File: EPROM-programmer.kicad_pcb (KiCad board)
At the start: 4 copper layers, 99.1 x 99.1 mm, 80 parts, among them J1 ZIF-socket, J10 VCC, J2 ISP, J5 GND, J6 Barrel_Jack_Switch, J7 ZIF_VCC, J8 VPP, J9 GND, P1 USB-C, Q1 BC327, Q2 BC327, Q3 BC327, Q4 BC327, Q5 BC327, Q6 BC327, SW1 SW_Push, U1 ATmega1284-P, U2 MCP2221AxP, U3 MCP4812, U4 LM358, U5 ULN2003, U6 LM317_TO-220, U7 LM317_TO-220, U8 R-78K9.0-0.5, Y1 20M

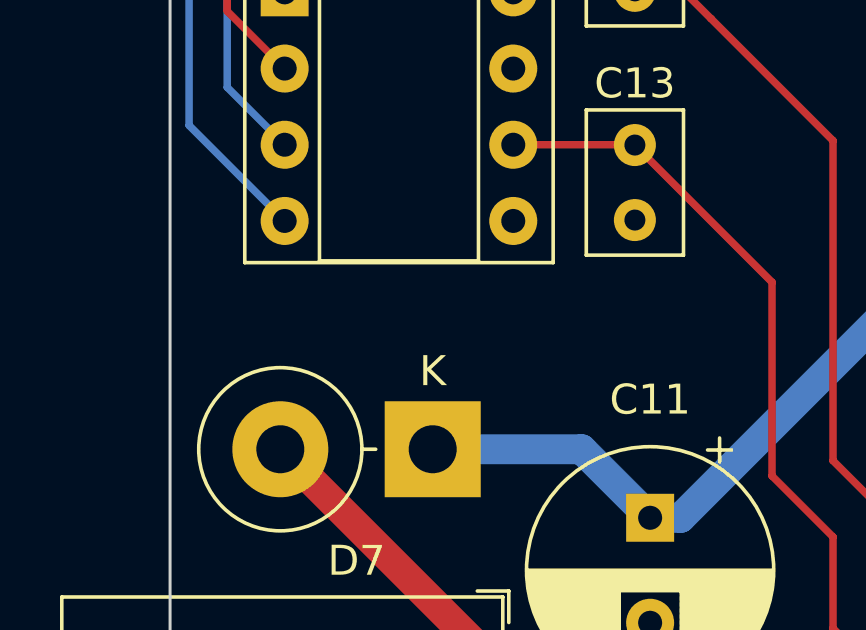
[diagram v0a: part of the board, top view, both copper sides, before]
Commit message: Add info about polarity and voltage to PCB
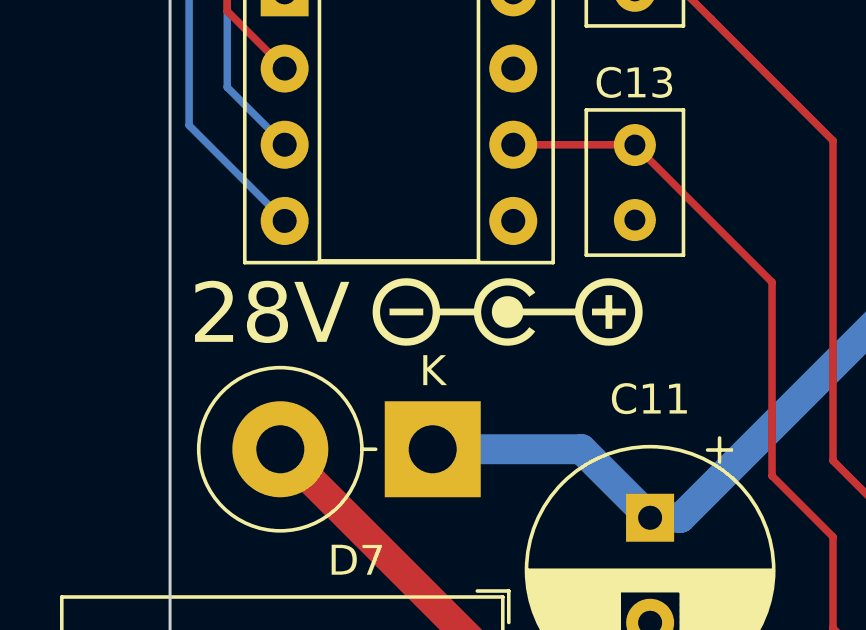
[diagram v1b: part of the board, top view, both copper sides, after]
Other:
- board text added: "28V"

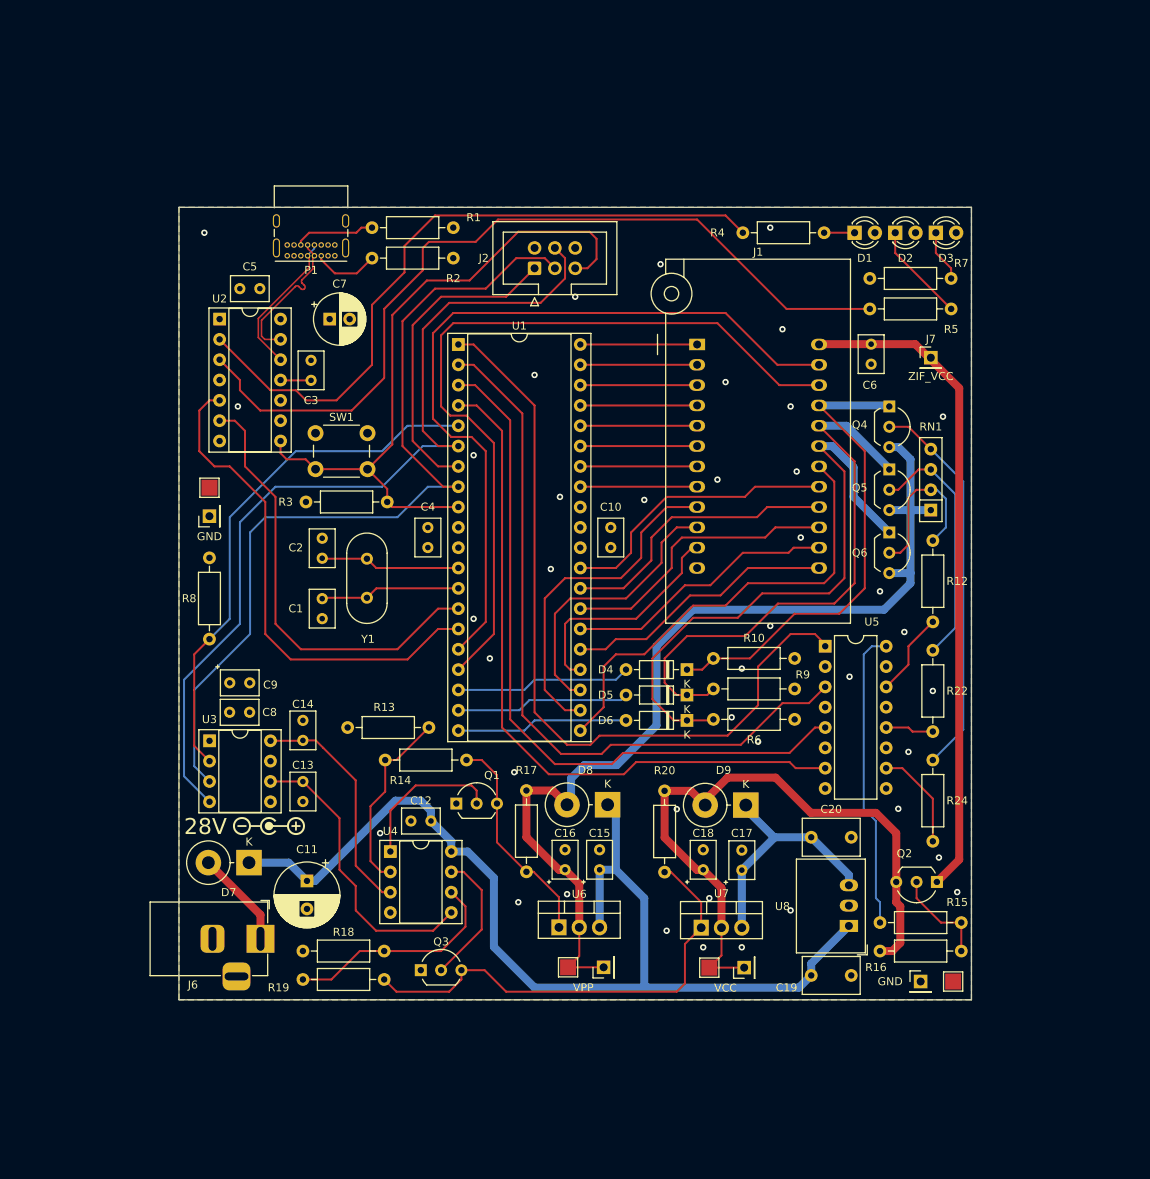
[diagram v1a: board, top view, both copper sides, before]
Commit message: Prepare for using 2 layers instead of 4
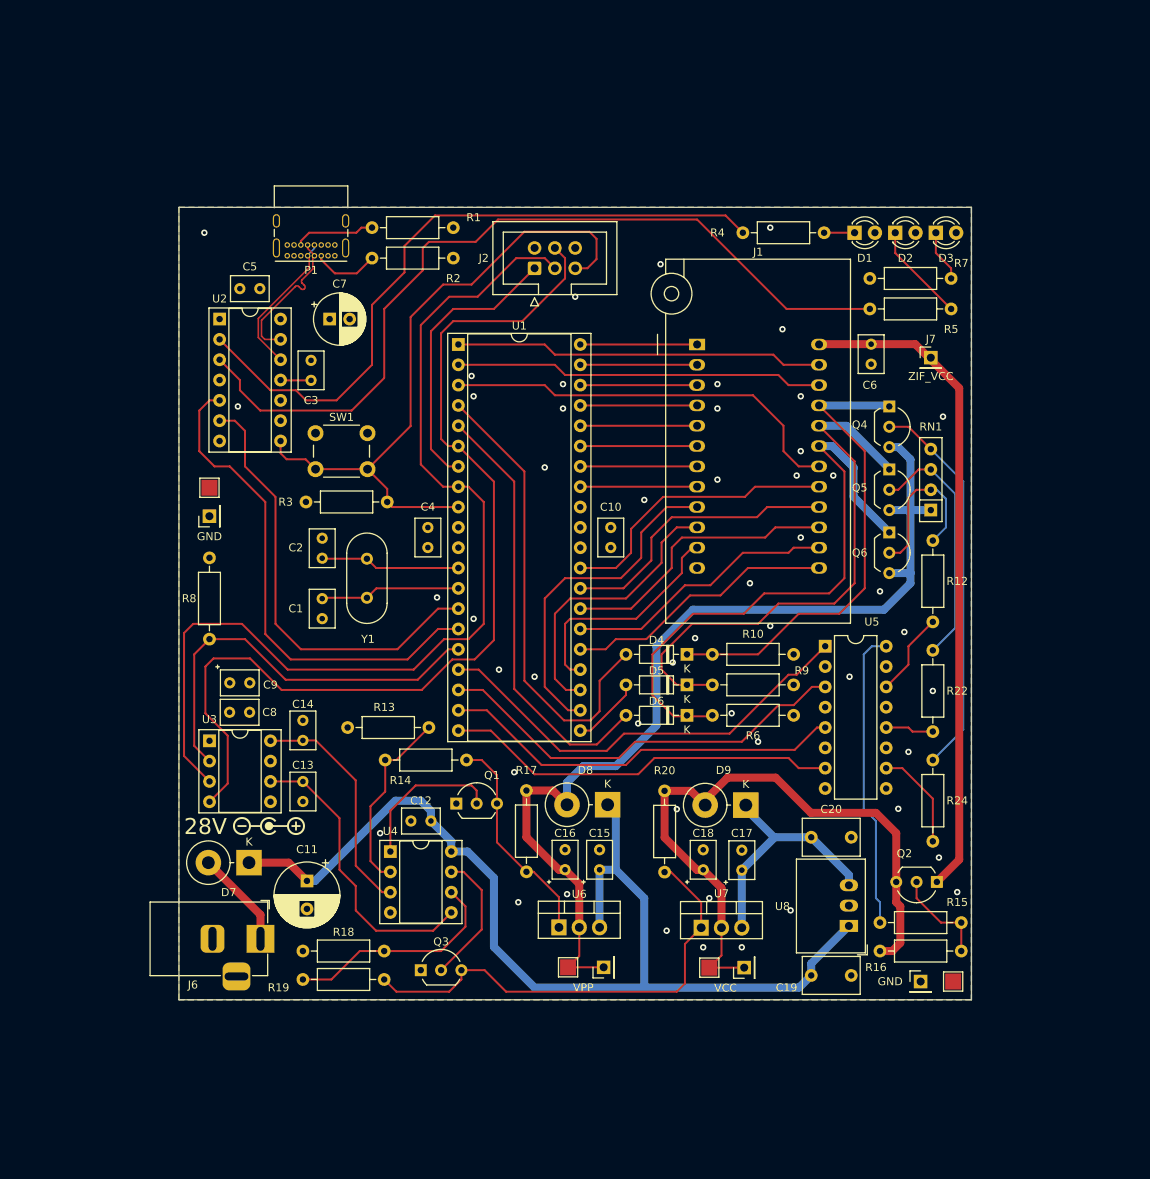
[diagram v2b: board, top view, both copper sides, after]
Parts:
- moved D4 1.91 mm to (102.9, 114.3)
- moved D5 1.27 mm to (102.9, 118.1)
- moved D6 0.64 mm to (102.9, 121.9)
- moved R10 0.52 mm to (106.0, 114.3)
- moved R6 0.52 mm to (106.0, 121.9)
- moved R9 0.52 mm to (106.0, 118.1)
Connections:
- U1 pad 1: /ZIF_VCC_EN -> /ZIF_P23
- U1 pad 16: /ZIF_P23 -> /~{SS}
- U1 pad 17: /ZIF_P22 -> /ZIF_VCC_EN
- U1 pad 18: /D_P21 -> /ZIF_VPP_P19_EN
- U1 pad 19: /D_P20 -> /ZIF_VPP_P20_EN
- U1 pad 2: /ZIF_VPP_P19_EN -> /ZIF_P22
- U1 pad 20: /D_P19 -> /ZIF_VPP_P21_EN
- U1 pad 21: /ZIF_P18 -> /D_P20
- U1 pad 3: /ZIF_VPP_P20_EN -> /ZIF_P18
- U1 pad 4: /ZIF_VPP_P21_EN -> /D_P21
- U1 pad 5: /~{SS} -> /D_P19
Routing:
- net /ZIF_P22: track 98.6 -> 46.1 mm
- net /ZIF_P23: track 97.1 -> 46.1 mm
- net /ZIF_VCC_EN: track 98.4 -> 55.5 mm
- net /ZIF_VPP_P20_EN: track 89.3 -> 50.6 mm
- net /ZIF_VPP_P19_EN: track 91.6 -> 53.1 mm
- net /ZIF_VPP_P21_EN: track 87.6 -> 49.5 mm
- net /D_P21: track 22.0 -> 58.2 mm
- net /D_P19: track 21.5 -> 54.1 mm
- net /SCK: track 110.8 -> 125.8 mm
- net /~{SS}: track 66.4 -> 51.6 mm
- net /D_P20: track 21.7 -> 8.83 mm
- net /MOSI: track 113.1 -> 124.2 mm
- net /ZIF_P18: track 57.0 -> 51.2 mm
- net /MISO: track 39.7 -> 35.3 mm
- net /~{RESET}: track 83.9 -> 82.4 mm
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
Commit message: Increase PCB size. Rework PCB to use 2 layers
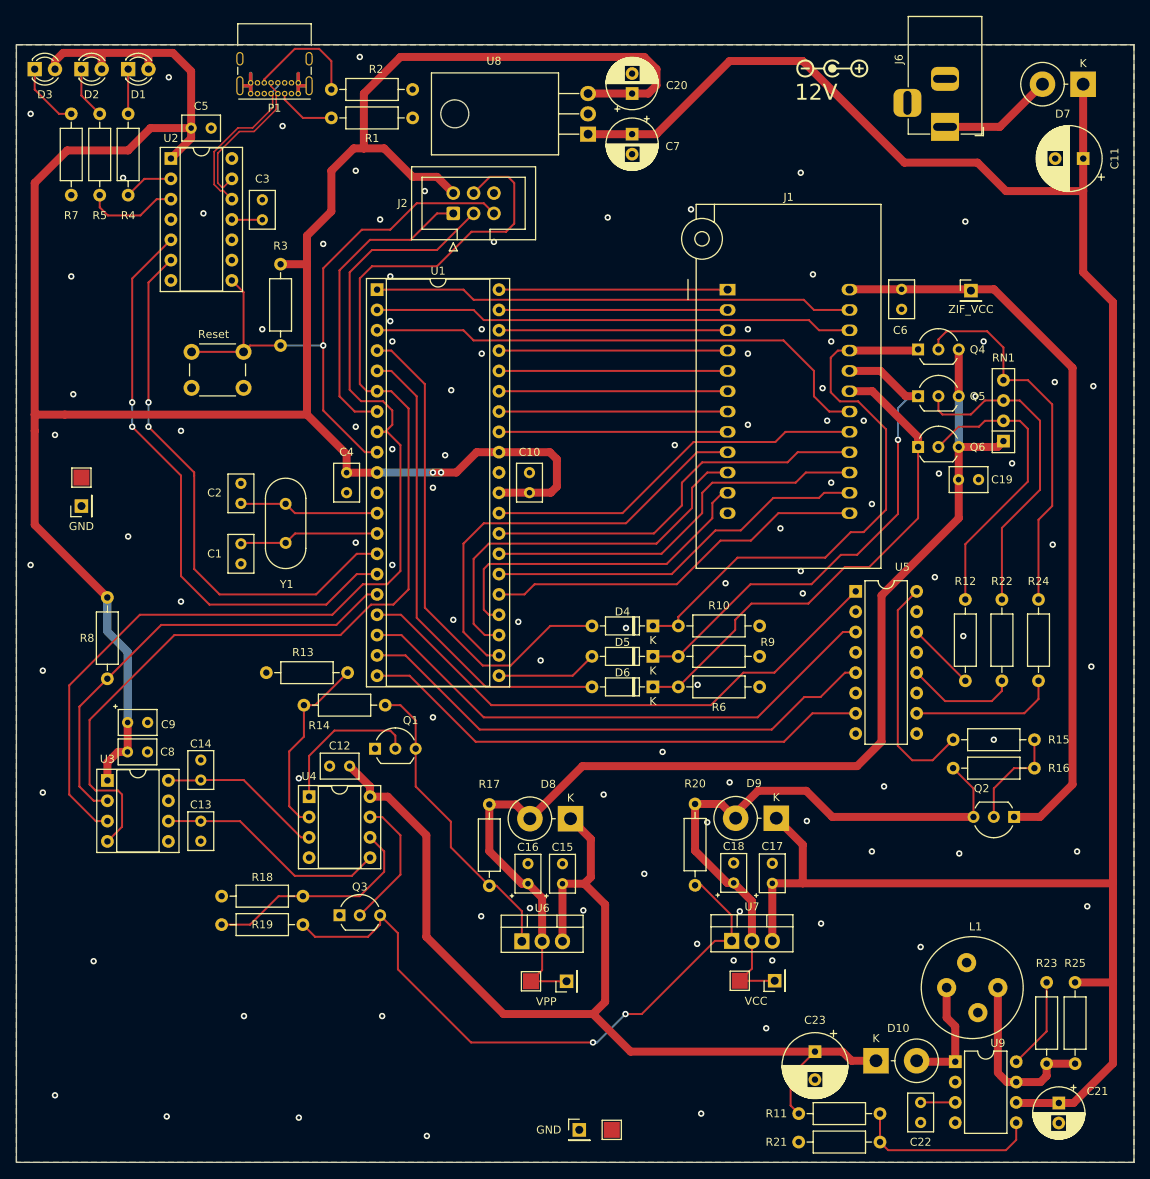
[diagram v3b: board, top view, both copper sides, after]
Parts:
- added C21: 100u, Capacitor_THT:CP_Radial_D6.3mm_P2.50mm, F.Cu at (149.4, 170.4)
- added C22: 270p, Capacitor_THT:C_Rect_L4.6mm_W3.0mm_P2.50mm_MKS02_FKP02, F.Cu at (132.1, 170.3)
- added C23: 330u, Capacitor_THT:CP_Radial_D8.0mm_P3.50mm, F.Cu at (118.9, 164.0)
- added D10: SB340, Diode_THT:D_DO-201AD_P5.08mm_Vertical_KathodeUp, F.Cu at (126.5, 165.1)
- added L1: 330u, Local:L_Radial_D12.5mm_P4.00mm_5.00mm, F.Cu at (140.7, 153.2)
- added R11: 22K1, Resistor_THT:R_Axial_DIN0207_L6.3mm_D2.5mm_P10.16mm_Horizontal, F.Cu at (127.0, 171.7)
- added R21: 1K, Resistor_THT:R_Axial_DIN0207_L6.3mm_D2.5mm_P10.16mm_Horizontal, F.Cu at (116.8, 175.3)
- added R23: 180, Resistor_THT:R_Axial_DIN0207_L6.3mm_D2.5mm_P10.16mm_Horizontal, F.Cu at (147.8, 155.3)
- added R25: R270, Resistor_THT:R_Axial_DIN0207_L6.3mm_D2.5mm_P10.16mm_Horizontal, F.Cu at (151.4, 155.3)
- added U9: MC34063AP, Package_DIP:DIP-8_W7.62mm, F.Cu at (136.4, 165.2)
- C19: value 10u -> 100n; footprint Capacitor_THT:C_Rect_L7.0mm_W4.5mm_P5.00mm -> Capacitor_THT:C_Rect_L4.6mm_W3.0mm_P2.50mm_MKS02_FKP02
- C20: value 22u -> 10u; footprint Capacitor_THT:C_Rect_L7.0mm_W4.5mm_P5.00mm -> Capacitor_THT:CP_Radial_D6.3mm_P2.50mm
- SW1: value SW_Push -> Reset
- U8: value R-78K9.0-0.5 -> LM7805_TO220; footprint Converter_DCDC:Converter_DCDC_RECOM_R-78E-0.5_THT -> Package_TO_SOT_THT:TO-220-3_Horizontal_TabDown
- moved D7 142.6 mm to (152.4, 43.0)
- moved J6 132.8 mm to (135.1, 48.4), turned to -90 degrees
- moved C11 132.5 mm to (152.4, 52.3), turned to 180 degrees
- moved D3 114.5 mm to (21.3, 41.1)
- moved R7 111.9 mm to (25.9, 46.7), turned to -90 degrees
- moved R5 109.2 mm to (29.5, 46.7), turned to -90 degrees
- moved U8 104.2 mm to (90.5, 49.3)
- moved D2 103.8 mm to (27.2, 41.1)
- moved C20 95.6 mm to (96.0, 44.2), turned to 90 degrees
- moved D1 93.1 mm to (33.0, 41.1)
- moved R4 88.3 mm to (33.0, 46.7), turned to -90 degrees
- moved C19 64.7 mm to (136.8, 92.5)
- moved J5 46.5 mm to (89.4, 173.7)
- moved TP3 46.5 mm to (93.5, 173.7)
- moved C7 44.3 mm to (96.0, 49.3), turned to -90 degrees
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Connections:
- net /28V_IN renamed /Power/12V_IN
- net /ADJ_VCC renamed /Power/ADJ_VCC
- net /ADJ_VPP renamed /Power/ADJ_VPP
- net /D+ renamed /Programmer/D+
- net /D- renamed /Programmer/D-
- net /DAC_VCC renamed /Power/DAC_VCC
- net /DAC_VPP renamed /Power/DAC_VPP
- net /D_P19 renamed /Programmer/D_P19
- net /D_P20 renamed /Programmer/D_P20
- net /D_P21 renamed /Programmer/D_P21
- net /FB_VCC renamed /Power/FB_VCC
- net /FB_VPP renamed /Power/FB_VPP
- net /MISO renamed /Programmer/MISO
- net /MOSI renamed /Programmer/MOSI
- net /RXD renamed /Programmer/RXD
- net /RXD_LED renamed /Programmer/RXD_LED
- net /SCK renamed /Programmer/SCK
- net /TXD renamed /Programmer/TXD
- net /TXD_LED renamed /Programmer/TXD_LED
- net /VCC renamed /Power/VCC
- net /XTAL1 renamed /Programmer/XTAL1
- net /XTAL2 renamed /Programmer/XTAL2
- net /ZIF_P1 renamed /Programmer/ZIF_P1
- net /ZIF_P10 renamed /Programmer/ZIF_P10
- net /ZIF_P11 renamed /Programmer/ZIF_P11
- net /ZIF_P13 renamed /Programmer/ZIF_P13
- net /ZIF_P14 renamed /Programmer/ZIF_P14
- net /ZIF_P15 renamed /Programmer/ZIF_P15
- net /ZIF_P16 renamed /Programmer/ZIF_P16
- net /ZIF_P17 renamed /Programmer/ZIF_P17
- net /ZIF_P18 renamed /Programmer/ZIF_P18
- net /ZIF_P19 renamed /Programmer/ZIF_P19
- net /ZIF_P2 renamed /Programmer/ZIF_P2
- net /ZIF_P20 renamed /Programmer/ZIF_P20
- net /ZIF_P21 renamed /Programmer/ZIF_P21
- net /ZIF_P22 renamed /Programmer/ZIF_P22
- net /ZIF_P23 renamed /Programmer/ZIF_P23
- net /ZIF_P3 renamed /Programmer/ZIF_P3
- net /ZIF_P4 renamed /Programmer/ZIF_P4
- net /ZIF_P5 renamed /Programmer/ZIF_P5
- net /ZIF_P6 renamed /Programmer/ZIF_P6
- net /ZIF_P7 renamed /Programmer/ZIF_P7
- net /ZIF_P8 renamed /Programmer/ZIF_P8
- net /ZIF_P9 renamed /Programmer/ZIF_P9
- net /ZIF_VCC renamed /Programmer/ZIF_VCC
- net /ZIF_VCC_EN renamed /Programmer/ZIF_VCC_EN
- net /ZIF_VPP_P19_EN renamed /Programmer/ZIF_VPP_P19_EN
- net /ZIF_VPP_P20_EN renamed /Programmer/ZIF_VPP_P20_EN
- net /ZIF_VPP_P21_EN renamed /Programmer/ZIF_VPP_P21_EN
- net /~{RESET} renamed /Programmer/~{RESET}
- net /~{SS} renamed /Power/~{SS}
- net /~{ZIF_VCC_EN} renamed /Programmer/~{ZIF_VCC_EN}
- net /~{ZIF_VPP_P19_EN} renamed /Programmer/~{ZIF_VPP_P19_EN}
- net /~{ZIF_VPP_P20_EN} renamed /Programmer/~{ZIF_VPP_P20_EN}
- net /~{ZIF_VPP_P21_EN} renamed /Programmer/~{ZIF_VPP_P21_EN}
- C11 pad 1: +28V -> +12V
- C16 pad 1: /VPP -> /Power/VPP
- C17 pad 1: +9V -> +12V
- C19 pad 1: +28V -> /Power/VPP
- C20 pad 1: +9V -> +5V
- C7 pad 1: +5V -> +12V
- D7 pad 1: +28V -> +12V
- D8 pad 2: /VPP -> /Power/VPP
- D9 pad 1: +9V -> +12V
- J8 pad 1: /VPP -> /Power/VPP
- P1 pad A4: +5V -> unconnected-(P1-VBUS-PadA4)_1
- P1 pad A5: /CC1 -> /Programmer/CC1
- P1 pad A9: +5V -> unconnected-(P1-VBUS-PadA4)_0
- P1 pad B4: +5V -> unconnected-(P1-VBUS-PadA4)_2
- P1 pad B5: /CC2 -> /Programmer/CC2
- P1 pad B9: +5V -> unconnected-(P1-VBUS-PadA4)
- Q4 pad 3: /VPP -> /Power/VPP
- Q5 pad 3: /VPP -> /Power/VPP
- Q6 pad 3: /VPP -> /Power/VPP
- R1 pad 1: /CC2 -> /Programmer/CC1
- R17 pad 1: /VPP -> /Power/VPP
- R2 pad 1: /CC1 -> /Programmer/CC2
- RN1 pad 1: /VPP -> /Power/VPP
- TP4 pad 1: /VPP -> /Power/VPP
- U6 pad 2: /VPP -> /Power/VPP
- U7 pad 3: +9V -> +12V
- U8 pad 1: +28V -> +12V
- U8 pad 3: +9V -> +5V
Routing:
- net +5V: track 9.11 -> 332.9 mm, vias 0 -> 2
- net +12V: track 0.00 -> 274.6 mm
- net /Power/VPP: track 0.00 -> 143.0 mm
- net /VPP: track 124.6 -> 0.00 mm
- net /Programmer/RXD_LED: track 105.9 -> 11.7 mm
- net /Programmer/TXD_LED: track 85.4 -> 6.19 mm
- net +9V: track 31.1 -> 0.00 mm
- net Net-(U9-Vfb): track 0.00 -> 23.7 mm
- net Net-(U9-Ipk): track 0.00 -> 22.6 mm
- net /Power/ADJ_VCC: track 58.7 -> 79.8 mm, vias 0 -> 2
- net /Programmer/MOSI: track 124.2 -> 142.5 mm
- net Net-(Q6-B): track 20.1 -> 37.5 mm
- net /Programmer/ZIF_VPP_P20_EN: track 50.6 -> 66.6 mm
- net /Programmer/ZIF_VPP_P19_EN: track 53.1 -> 68.5 mm
- net /Programmer/ZIF_VPP_P21_EN: track 49.5 -> 64.7 mm
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- removed copper zone on In1.Cu, net +5V
- removed copper zone on In2.Cu, net GND
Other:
- board size 99.1 x 99.1 mm -> 139.7 x 139.7 mm
- copper layers 4 -> 2
- board text added: "12V"
- board text removed: "28V"
